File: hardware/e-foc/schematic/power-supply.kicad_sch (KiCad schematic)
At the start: 26 parts, among them U4 LM5164DDA, U5 AMS1117-3.3

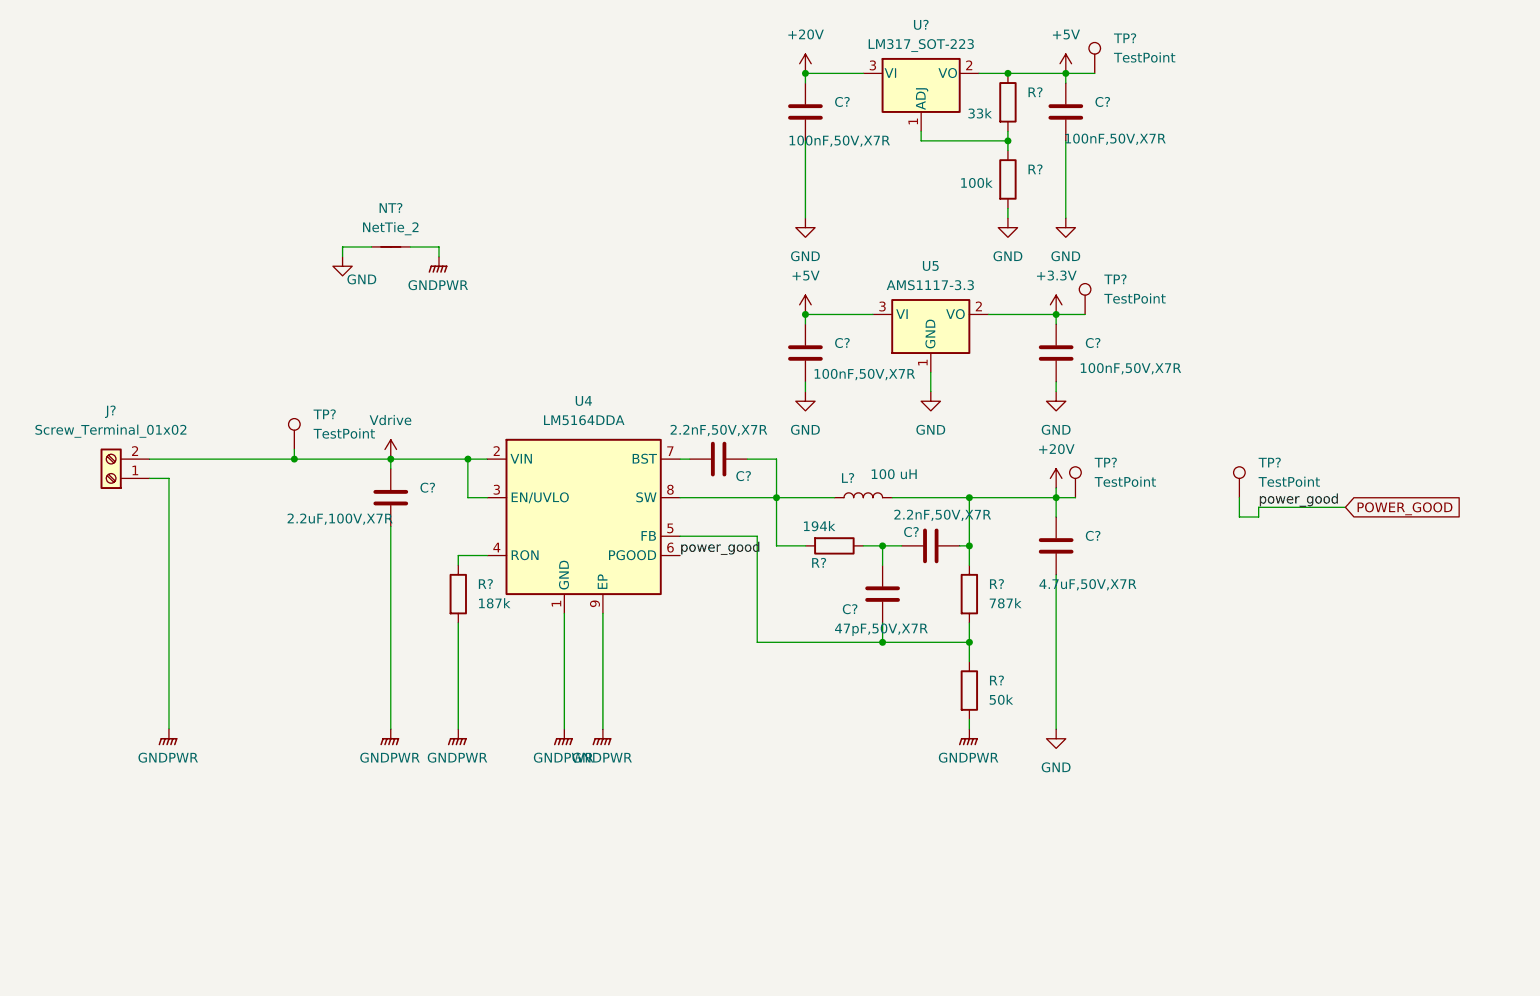
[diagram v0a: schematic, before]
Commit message: chore: add release please action (#1)
* add release please action

* refactor structure

* schematic finished

* pcb improvements

* board finished

* updates

* updates

* .\.claude\

* updates

* reorganize project

* fix ci

* fix ci

* fix(ci): disable kicad-bot bom/diff (not implemented in v0.1.3)

verify (ERC/DRC) passes, but run-bom-check and run-diff exit 2 with
"not available in this build yet (Phase 2/3)". Keep run-verify only.

Co-Authored-By: Claude Opus 4.8 <noreply@anthropic.com>

* feat(ci): visual schematic/PCB diff on pull requests

kicad-bot's diff phase isn't available in v0.1.x, so render PR head vs base
with kicad-cli and produce a red/green overlay (added/removed) per board via
Pillow — no KiAuto/GUI automation. New scripts/visual_diff.py + a matrix
kicad-diff.yml that uploads the diff images as a per-board artifact.

Co-Authored-By: Claude Opus 4.8 <noreply@anthropic.com>

* fix(erc): ignore power_pin_not_driven instead of per-instance exclusions

Both boards are powered through a connector, so power_pin_not_driven is an
expected false-positive. It was suppressed via GUI per-instance exclusions
(hashed by coordinates/UUIDs), which don't survive a different KiCad patch or
the PR merge commit in CI -> the violations resurfaced as ERC errors and
failed verify (e.g. tiva: 4 errors). Set the rule severity to "ignore" in
each .kicad_pro: deterministic, committed, version-independent. 0 ERC errors
on both boards now.

Co-Authored-By: Claude Opus 4.8 <noreply@anthropic.com>

---------

Co-authored-by: Claude Opus 4.8 <noreply@anthropic.com>
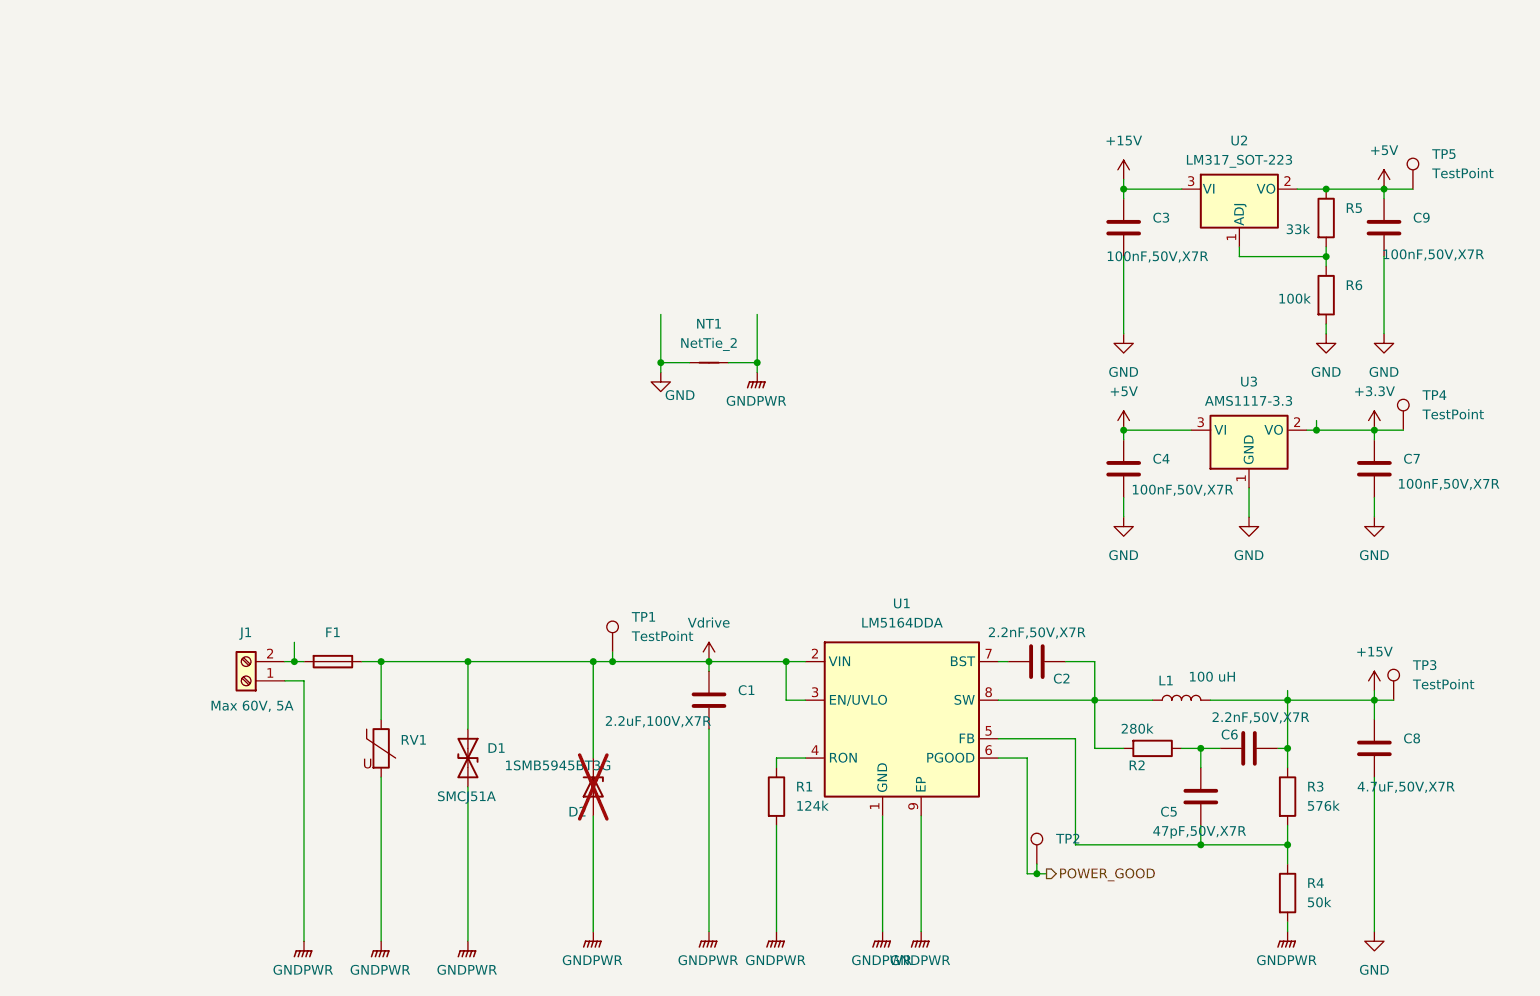
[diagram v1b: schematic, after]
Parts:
- added D1: SMCJ51A, Diode_SMD:D_SMC, symbol Device:D_TVS
- added D2: 1SMB5945BT3G, Diode_SMD:D_SMB, symbol Device:D_Zener
- added F1: Fuse, Fuse:Fuse_1812_4532Metric, symbol Device:Fuse
- added RV1: Varistor, Fuse:Fuse_1812_4532Metric, symbol Device:Varistor
- C1, C2, C3, C4, C5, C6, C7, C8, C9: renamed from C?; footprint (none) -> Capacitor_SMD:C_0805_2012Metric_Pad1.18x1.45mm_HandSolder
- J1: renamed from J?; footprint TerminalBlock:TerminalBlock_Xinya_XY308-2.54-2P_1x02_P2.54mm_Horizontal -> TerminalBlock_CUI:TerminalBlock_CUI_TB007-508-02_1x02_P5.08mm_Horizontal; Usage (none) -> Max 60V, 5A
- L1: renamed from L?; footprint Inductor_SMD:L_12x12mm_H8mm -> Inductor_SMD:L_7.3x7.3_H4.5
- R1: renamed from R?; value 187k -> 124k
- R2: renamed from R?; value 194k -> 280k
- R3: renamed from R?; value 787k -> 576k
- U1: renamed from U4; footprint Package_SO:HSOP-8-1EP_3.9x4.9mm_P1.27mm_EP2.41x3.1mm_ThermalVias -> Package_SO:HSOP-8-1EP_3.9x4.9mm_P1.27mm_EP2.41x3.1mm
- gave numbers to parts that had none: 10
- renumbered U5 to U3
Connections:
- net GNDPWR: now also D1.2 (A2), D2.2 (A), RV1.2
- net Vdrive: now also D1.1 (A1), D2.1 (K), F1.1, RV1.1; no longer J1.2 (Pin_2)
- net +20V renamed +15V
- new net: F1.2, J1.2 (Pin_2)
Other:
- moved on the sheet: C1, C2, C3, C4, C5, C6, C7, C8, C9, J1, L1, NT1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
